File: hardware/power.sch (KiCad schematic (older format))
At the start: 0 parts

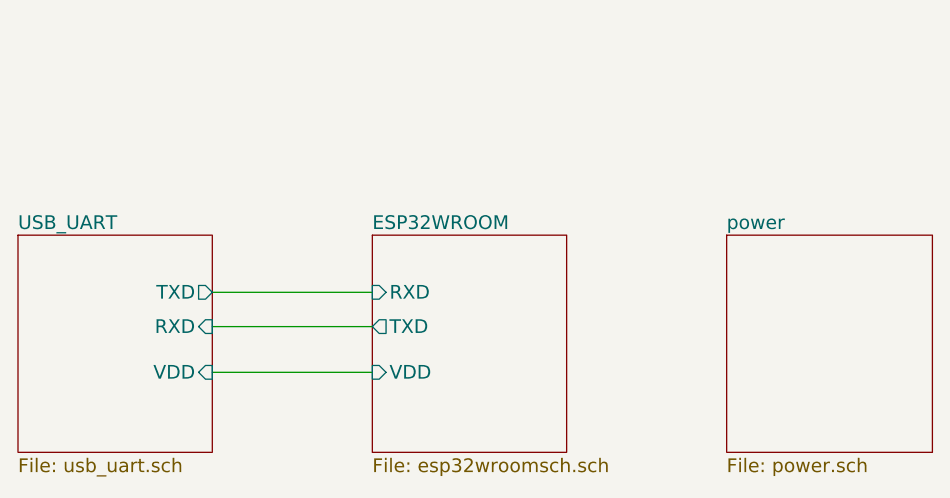
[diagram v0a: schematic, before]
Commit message: Add power sheet and BQ24266 to my library.
Signed-off-by: Kamil Gardziejczyk <kamil.gardziejczyk@firmwave.com>
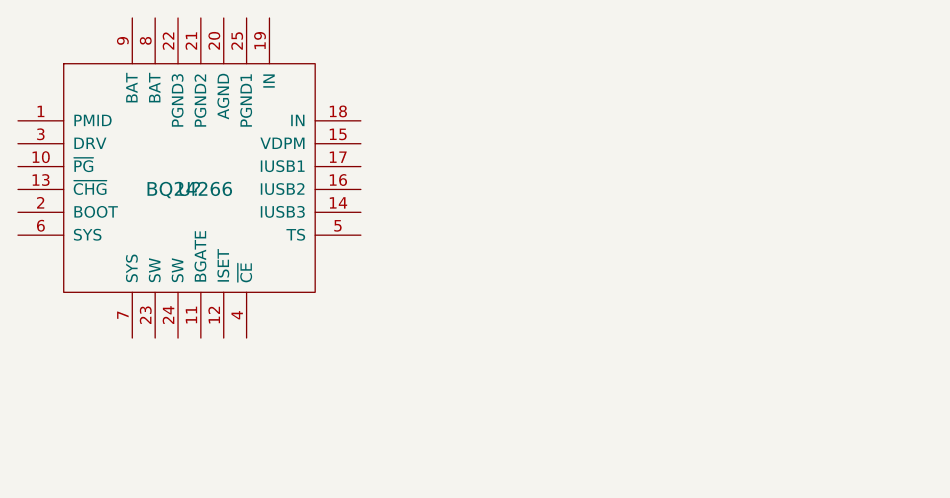
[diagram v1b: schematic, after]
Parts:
- added U?: BQ24266, symbol BQ24266
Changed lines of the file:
@@
 $Descr A4 11693 8268
 encoding utf-8
-Sheet 1 4
+Sheet 4 4
 Title ""
 Date ""
@@
 Comment4 ""
 $EndDescr
-$Sheet
-S 2750 2850 850  950
-U 597CE1AF
-F0 "USB_UART" 60
-F1 "usb_uart.sch" 60
-F2 "TXD" O R 3600 3100 60
-F3 "RXD" I R 3600 3250 60
-F4 "VDD" I R 3600 3450 60
-$EndSheet
-$Sheet
-S 4300 2850 850  950
-U 597CE33F
-F0 "ESP32WROOM" 60
-F1 "esp32wroomsch.sch" 60
-F2 "TXD" O L 4300 3250 60
-F3 "RXD" I L 4300 3100 60
-F4 "VDD" I L 4300 3450 60
-$EndSheet
-Wire Wire Line
-	3600 3100 4300 3100
-Wire Wire Line
-	3600 3250 4300 3250
-Wire Wire Line
-	3600 3450 4300 3450
-$Sheet
-S 5850 2850 900  950
-U 59862CC8
-F0 "power" 60
-F1 "power.sch" 60
-$EndSheet
+$Comp
+L BQ24266 U?
+U 1 1 598635CC
+P 3500 2600
+F 0 "U?" H 3500 2550 60  0000 C CNN
+F 1 "BQ24266" H 3500 2550 60  0000 C CNN
+F 2 "" H 3500 2550 60  0001 C CNN
+F 3 "" H 3500 2550 60  0001 C CNN
+	1    3500 2600
+	1    0    0    -1
+$EndComp
 $EndSCHEMATC

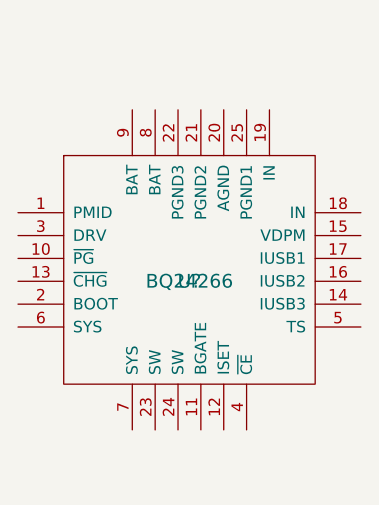
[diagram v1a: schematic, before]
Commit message: Added BQ24266 to power sheet.
Signed-off-by: Kamil Gardziejczyk <kamil.gardziejczyk@firmwave.com>
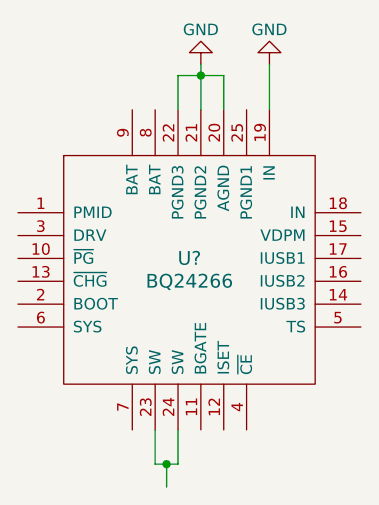
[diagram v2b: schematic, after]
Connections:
- net labels added: GND
- wire segments 0 -> 9
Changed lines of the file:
@@
 U 1 1 598635CC
 P 3500 2600
-F 0 "U?" H 3500 2550 60  0000 C CNN
+F 0 "U?" H 3500 2650 60  0000 C CNN
 F 1 "BQ24266" H 3500 2550 60  0000 C CNN
 F 2 "" H 3500 2550 60  0001 C CNN
@@
 	1    0    0    -1
 $EndComp
+$Comp
+L GND #PWR?
+U 1 1 59863804
+P 3550 1700
+F 0 "#PWR?" H 3550 1450 50  0001 C CNN
+F 1 "GND" H 3550 1550 50  0000 C CNN
+F 2 "" H 3550 1700 50  0001 C CNN
+F 3 "" H 3550 1700 50  0001 C CNN
+	1    3550 1700
+	-1   0    0    1
+$EndComp
+Wire Wire Line
+	3450 1750 3450 1900
+Wire Wire Line
+	3450 1750 3650 1750
+Wire Wire Line
+	3650 1750 3650 1900
+Wire Wire Line
+	3550 1700 3550 1900
+Connection ~ 3550 1750
+Wire Wire Line
+	3850 1900 3850 1700
+$Comp
+L GND #PWR?
+U 1 1 598638A3
+P 3850 1700
+F 0 "#PWR?" H 3850 1450 50  0001 C CNN
+F 1 "GND" H 3850 1550 50  0000 C CNN
+F 2 "" H 3850 1700 50  0001 C CNN
+F 3 "" H 3850 1700 50  0001 C CNN
+	1    3850 1700
+	-1   0    0    1
+$EndComp
+Wire Wire Line
+	3350 3300 3350 3450
+Wire Wire Line
+	3350 3450 3450 3450
+Wire Wire Line
+	3450 3450 3450 3300
+Wire Wire Line
+	3400 3450 3400 3550
+Connection ~ 3400 3450
 $EndSCHEMATC

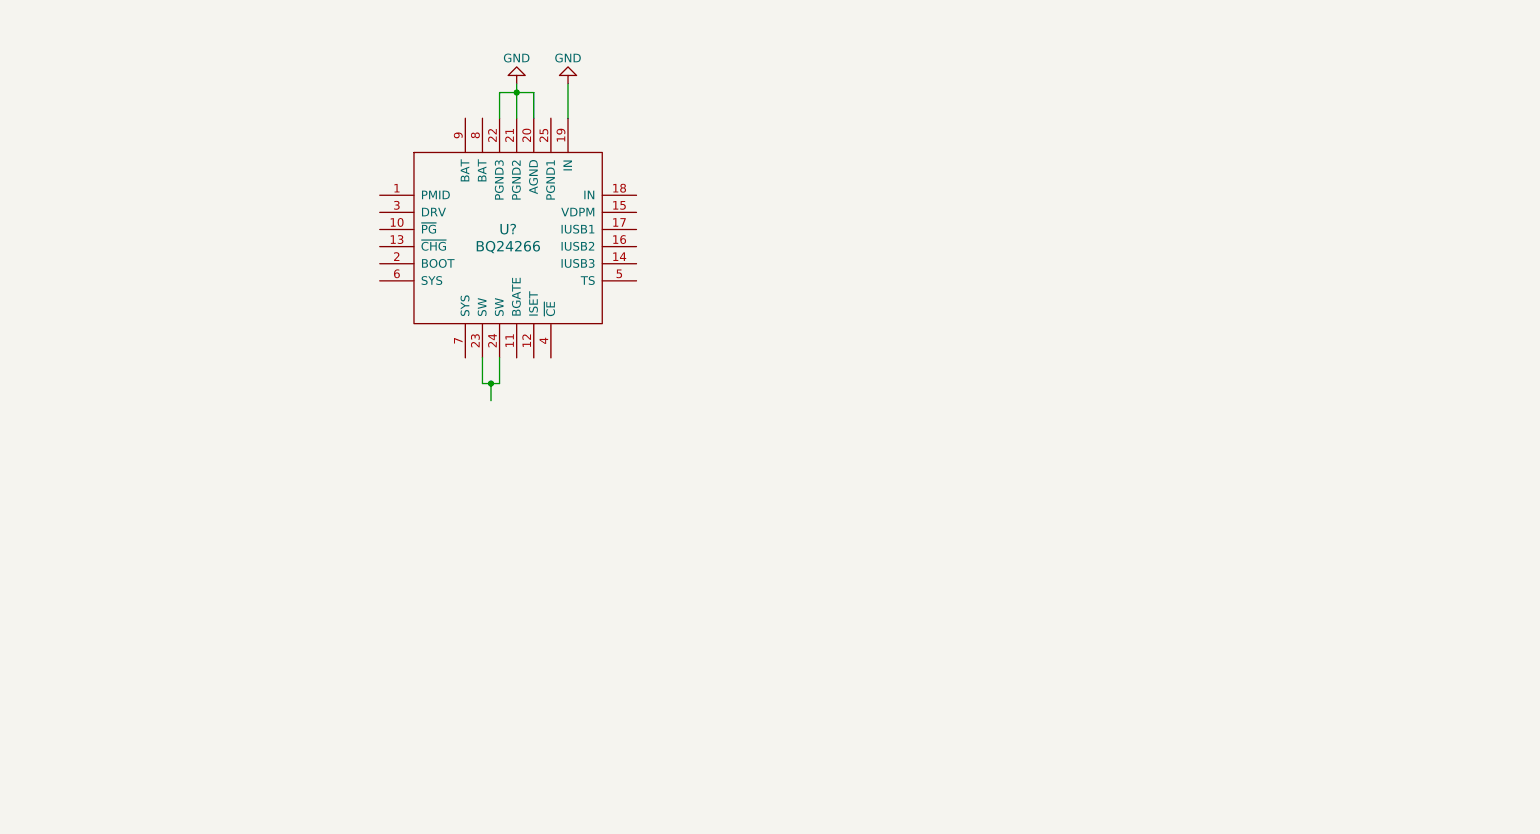
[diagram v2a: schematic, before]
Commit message: BQ24771 connected.
Signed-off-by: Kamil Gardziejczyk <kamil.gardziejczyk@firmwave.com>
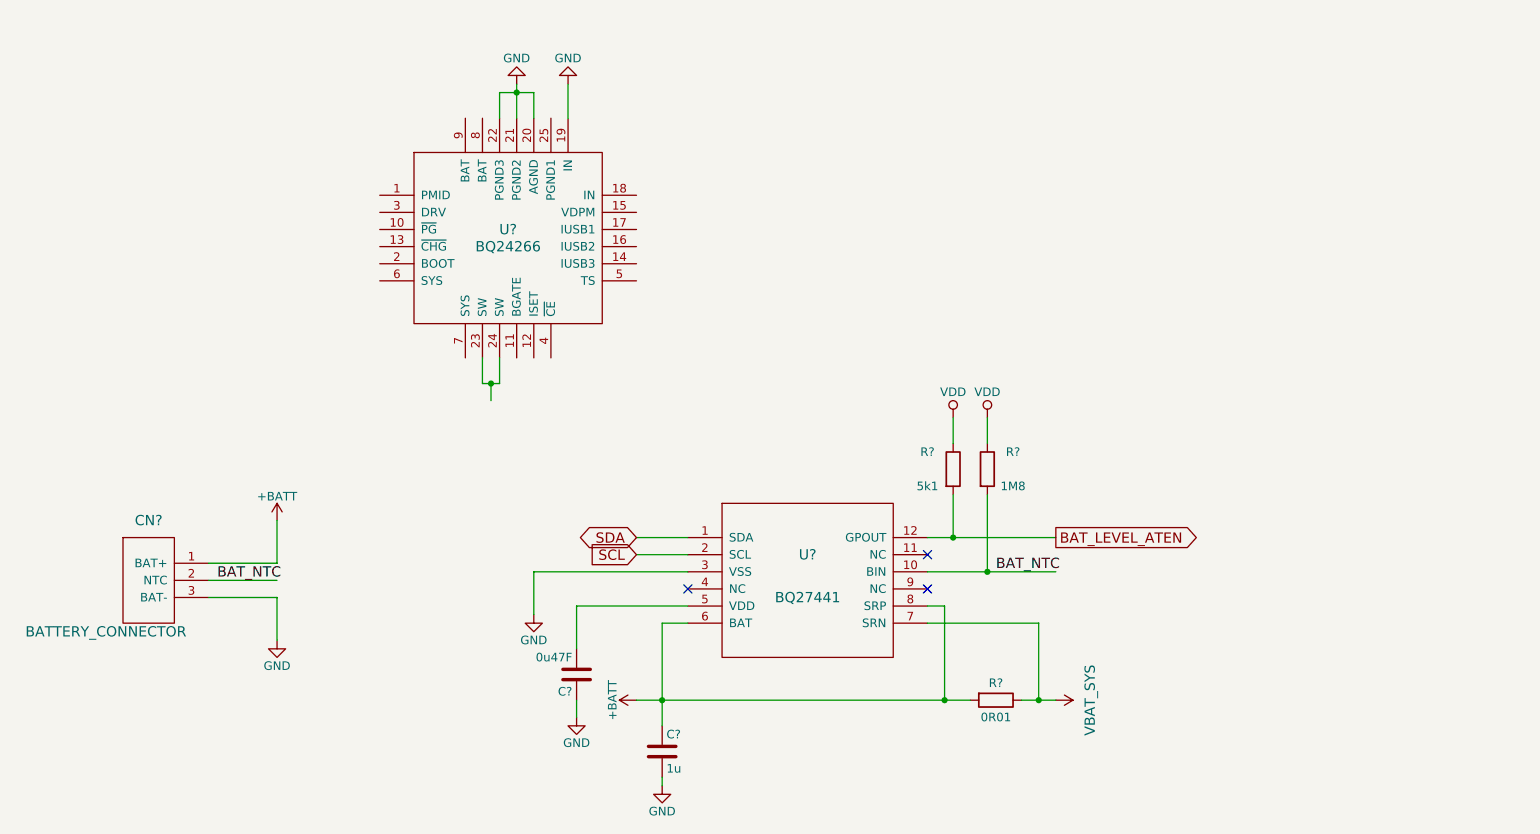
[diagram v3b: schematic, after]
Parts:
- added C?: 1u, symbol C
- added C?: 0u47F, symbol C
- added CN?: BATTERY_CONNECTOR, symbol BATTERY_CONNECTOR
- added PWR?: VBAT_SYS, symbol VBAT_SYS
- added R?: 5k1, symbol R
- added R?: 1M8, symbol R
- added R?: 0R01, symbol R
- added U?: BQ27441, symbol BQ27441
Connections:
- net labels added: +BATT, BAT_LEVEL_ATEN, BAT_NTC, SCL, SDA, VDD
- wire segments 9 -> 36
- no-connect marks 0 -> 3

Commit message: Adding missing connections for battery charger IC.
Signed-off-by: Kamil Gardziejczyk <kamil.gardziejczyk@firmwave.com>
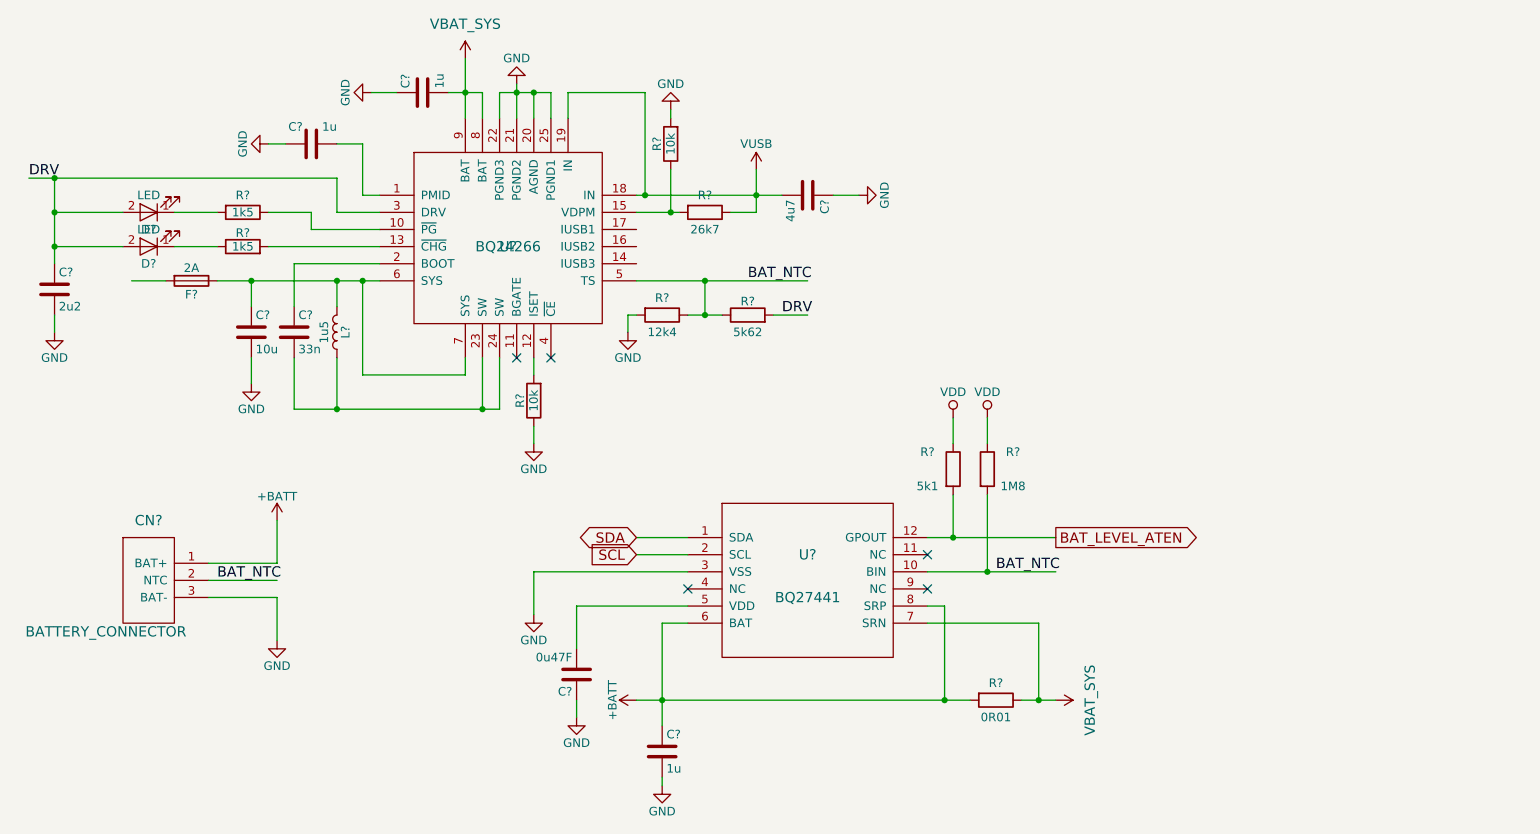
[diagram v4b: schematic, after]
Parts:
- removed U?: BQ24266, symbol BQ24266
- added C? (x2): 1u, symbol C
- added C?: 4u7, symbol C
- added C?: 2u2, symbol C
- added C?: 33n, symbol C
- added C?: 10u, symbol C
- added D? (x2): LED, symbol LED
- added F?: 2A, symbol Fuse
- added L?: 1u5, symbol L
- added PWR?: VBAT_SYS, symbol VBAT_SYS
- added R? (x2): 10k, symbol R
- added R?: 26k7, symbol R
- added R? (x2): 1k5, symbol R
- added R?: 12k4, symbol R
- added R?: 5k62, symbol R
- added U?: BQ24266, symbol BQ24266
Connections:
- net labels added: DRV, VUSB
- wire segments 36 -> 86
- no-connect marks 3 -> 5

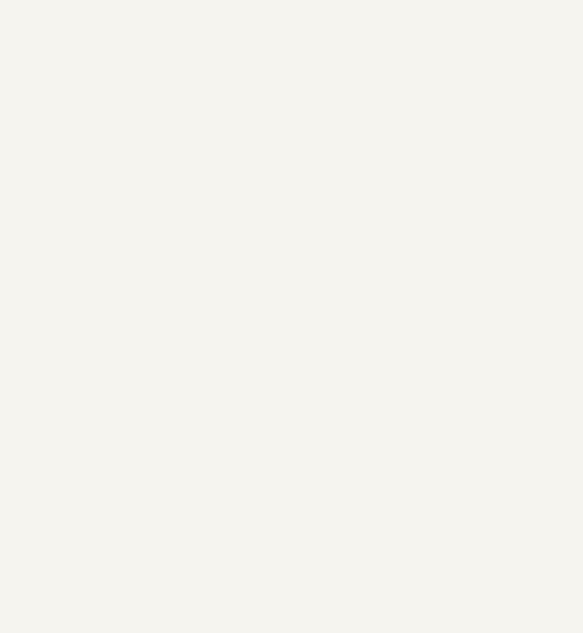
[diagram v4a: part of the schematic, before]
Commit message: Adding TPS63020 to library.
Signed-off-by: Kamil Gardziejczyk <kamil.gardziejczyk@firmwave.com>
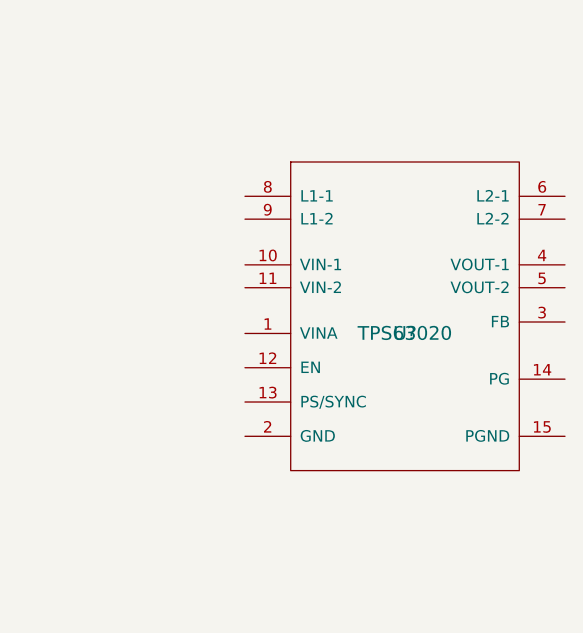
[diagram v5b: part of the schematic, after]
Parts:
- added U?: TPS63020, symbol TPS63020
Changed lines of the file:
@@
 $EndComp
 NoConn ~ 3750 3300
+$Comp
+L TPS63020 U?
+U 1 1 598CC7F3
+P 8750 2750
+F 0 "U?" H 8750 2750 60  0000 C CNN
+F 1 "TPS63020" H 8750 2750 60  0000 C CNN
+F 2 "" H 8750 2750 60  0001 C CNN
+F 3 "" H 8750 2750 60  0001 C CNN
+	1    8750 2750
+	1    0    0    -1
+$EndComp
 $EndSCHEMATC
